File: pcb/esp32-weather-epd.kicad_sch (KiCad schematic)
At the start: 67 parts, among them J1 S2B-PH-K-S(LF)(SN), Q1 S8050, Q2 S8050, Q3 BRCS150P02ZJ, Q4 SI1308EDL-T1-GE3, U1 CH340X, U2 TP4056X, U3 RT9080-33GJ5, U4 ESP32-WROOM-32E, U5 BME680

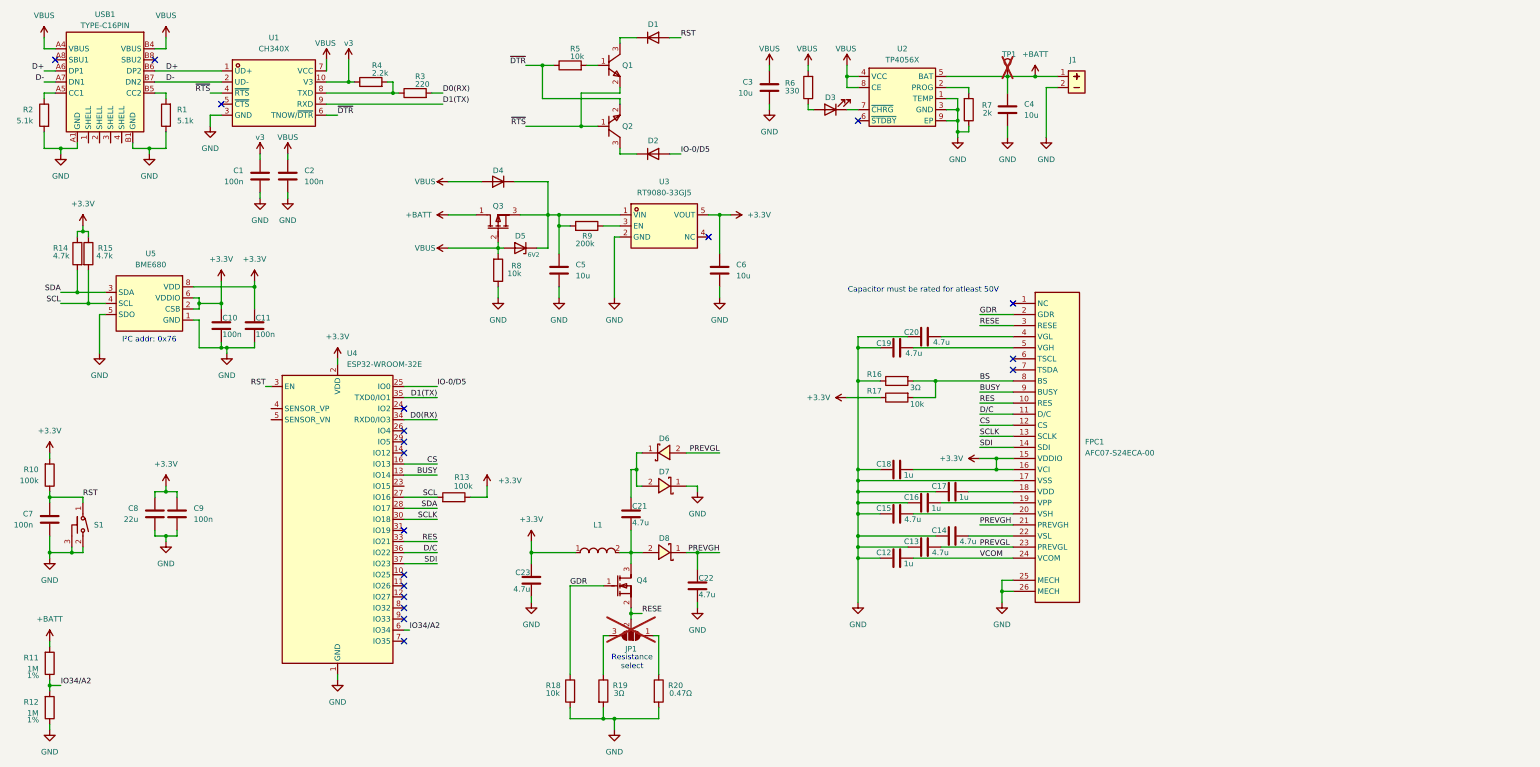
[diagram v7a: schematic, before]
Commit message: rework schematic and first draft component placement
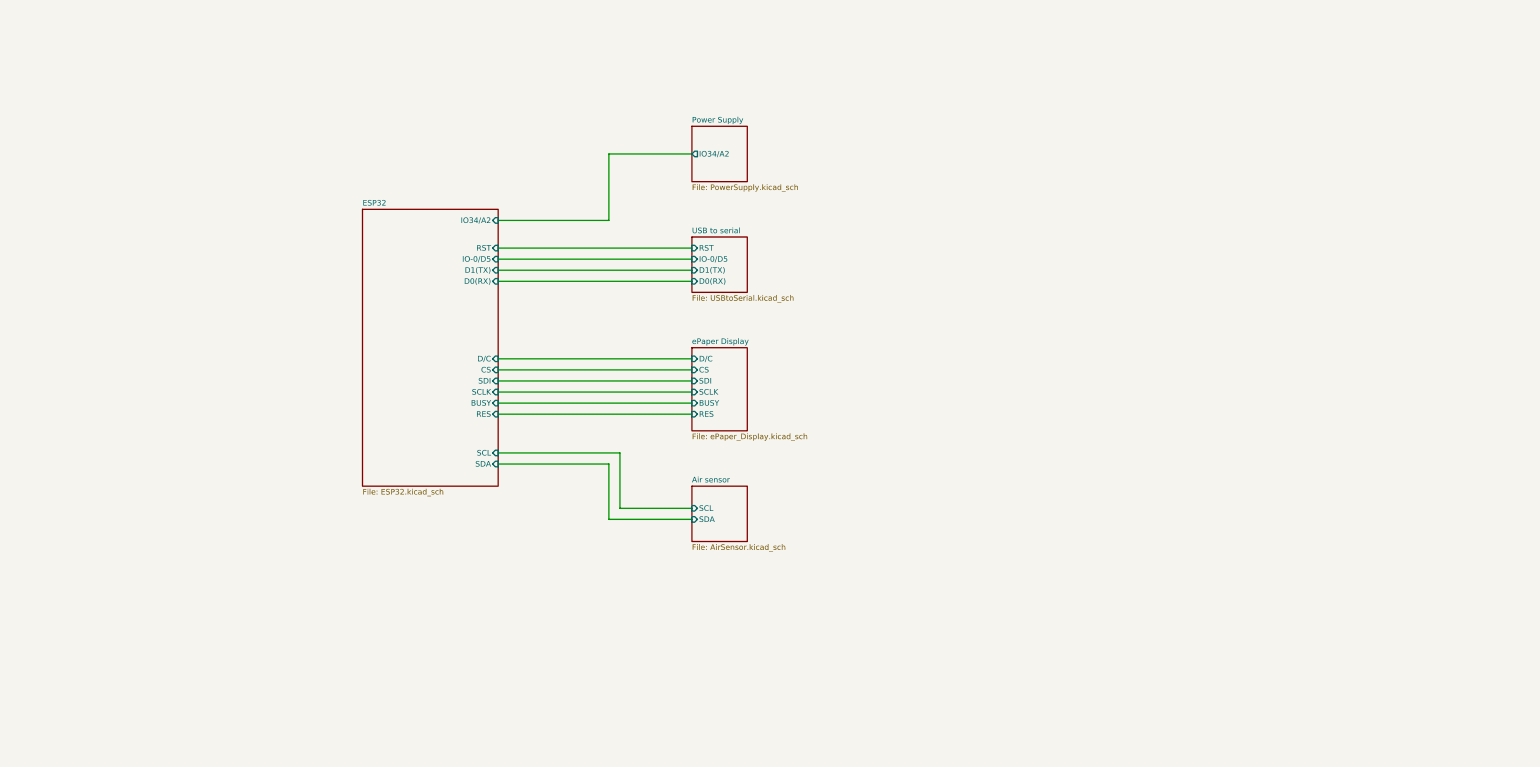
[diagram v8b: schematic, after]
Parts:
- removed C1, C10, C11, C2, C7, C9: 100n, Capacitor_SMD:C_0603_1608Metric, symbol Device:C
- removed C12, C16, C17, C18: 1u, Capacitor_SMD:C_0603_1608Metric, symbol Device:C
- removed C13, C14, C15, C19, C20, C21, C22, C23: 4.7u, Capacitor_SMD:C_0805_2012Metric, symbol Device:C
- removed C3, C4, C5, C6: 10u, Capacitor_SMD:C_0603_1608Metric, symbol Device:C
- removed C8: 22u, Capacitor_SMD:C_0603_1608Metric, symbol Device:C
- removed D1, D2: 1N4148, Diode_SMD:D_SOD-323, symbol Device:D
- removed D3: C397045, LED_SMD:LED_0402_1005Metric, symbol Device:LED
- removed D4: 1N5819, Diode_SMD:D_SOD-123F, symbol Device:D
- removed D5: LM3Z6V2T1G, Diode_SMD:D_SOD-323, symbol Device:D_Zener
- removed D6, D7, D8: MBR0530T1G, 0_local_lib:SOD-123_L2.7-W1.6-LS3.7-RD-1, symbol 0_local_lib:MBR0530T1G
- removed FPC1: AFC07-S24ECA-00, 0_local_lib:FPC-SMD_AFC07-S24ECA-00, symbol 0_local_lib:AFC07-S24ECA-00
- removed J1: S2B-PH-K-S(LF)(SN), 0_local_lib:CONN-TH_S2B-PH-K-S-LF-SN, symbol 0_local_lib:S2B-PH-K-S(LF)(SN)
- removed JP1: Resistanceselect, Jumper:SolderJumper-3_P1.3mm_Open_RoundedPad1.0x1.5mm_NumberLabels, symbol Jumper:SolderJumper_3_Open
- removed L1: CKCSA3010-10UH/M, 0_local_lib:IND-SMD_L3.0-W3.0-1, symbol 0_local_lib:CKCSA3010-10UH_M
- removed Q1, Q2: S8050, 0_local_lib:SOT-23-3_L2.9-W1.6-P1.90-LS2.8-BR, symbol 0_local_lib:S8050_C181158
- removed Q3: BRCS150P02ZJ, 0_local_lib:DFN-6L_L2.0-W2.0-P0.65-BL_BRCS300PXX, symbol 0_local_lib:BRCS150P02ZJ
- removed Q4: SI1308EDL-T1-GE3, 0_local_lib:SOT-323_L2.0-W1.3-P1.30-LS2.1-BR, symbol 0_local_lib:SI1308EDL-T1-GE3
- removed R1, R2: 5.1k, Resistor_SMD:R_0603_1608Metric, symbol Device:R
- removed R10, R13: 100k, Resistor_SMD:R_0603_1608Metric, symbol Device:R
- removed R11, R12: 1M, Resistor_SMD:R_0603_1608Metric, symbol Device:R
- removed R14, R15: 4.7k, Resistor_SMD:R_0603_1608Metric, symbol Device:R
- removed R16, R19: 3Ω, Resistor_SMD:R_0603_1608Metric, symbol Device:R
- removed R17, R18, R5, R8: 10k, Resistor_SMD:R_0603_1608Metric, symbol Device:R
- removed R20: 0.47Ω, Resistor_SMD:R_0603_1608Metric, symbol Device:R
- removed R3: 220, Resistor_SMD:R_0603_1608Metric, symbol Device:R
- removed R4: 2.2k, Resistor_SMD:R_0603_1608Metric, symbol Device:R
- removed R6: 330, Resistor_SMD:R_0603_1608Metric, symbol Device:R
- removed R7: 2k, Resistor_SMD:R_0603_1608Metric, symbol Device:R
- removed R9: 200k, Resistor_SMD:R_0603_1608Metric, symbol Device:R
- removed S1: YTS1C0033BBG01, 0_local_lib:SW-SMD_YIYUAN_YTS1C003XXX, symbol 0_local_lib:YTS1C0033BBG01
- removed TP1: TestPoint, TestPoint:TestPoint_Pad_D1.0mm, symbol Connector:TestPoint
- removed U1: CH340X, 0_local_lib:MSOP-10_L3.0-W3.0-P0.50-LS5.0-BL, symbol 0_local_lib:CH340X
- removed U2: TP4056X, 0_local_lib:SOP-8_L4.9-W3.9-P1.27-LS6.0-TL-EP, symbol 0_local_lib:TP4056X
- removed U3: RT9080-33GJ5, 0_local_lib:SOT-23-5_L3.0-W1.5-P0.95-LS2.8-BL, symbol 0_local_lib:RT9080-33GJ5
- removed U4: ESP32-WROOM-32E, RF_Module:ESP32-WROOM-32D, symbol RF_Module:ESP32-WROOM-32E
- removed U5: BME680, 0_local_lib:LGA-8_L3.0-W3.0-P0.80-TR, symbol 0_local_lib:BME680
- removed USB1: TYPE-C16PIN, 0_local_lib:USB-C-SMD_TYPE-C16PIN, symbol 0_local_lib:TYPE-C16PIN
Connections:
- no-connect marks 19 -> 0
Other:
- added sheet Air sensor (AirSensor.kicad_sch)
- added sheet ESP32 (ESP32.kicad_sch)
- added sheet Power Supply (PowerSupply.kicad_sch)
- added sheet USB to serial (USBtoSerial.kicad_sch)
- added sheet ePaper Display (ePaper_Display.kicad_sch)
- note removed: "Capacitor must be rated for atleast 50V"
- note removed: "I²C addr: 0x76"
- note removed: "Resistance select"
